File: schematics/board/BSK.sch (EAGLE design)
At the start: 56 parts

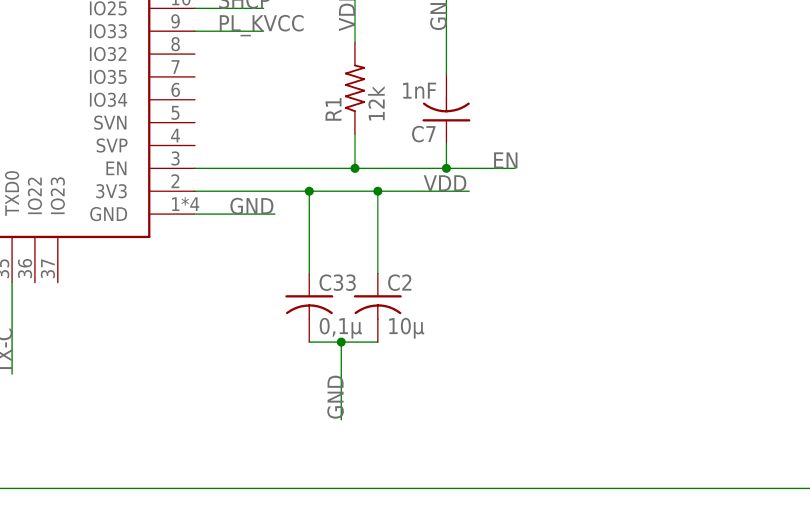
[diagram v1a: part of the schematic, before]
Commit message: Разведена плата БСК1
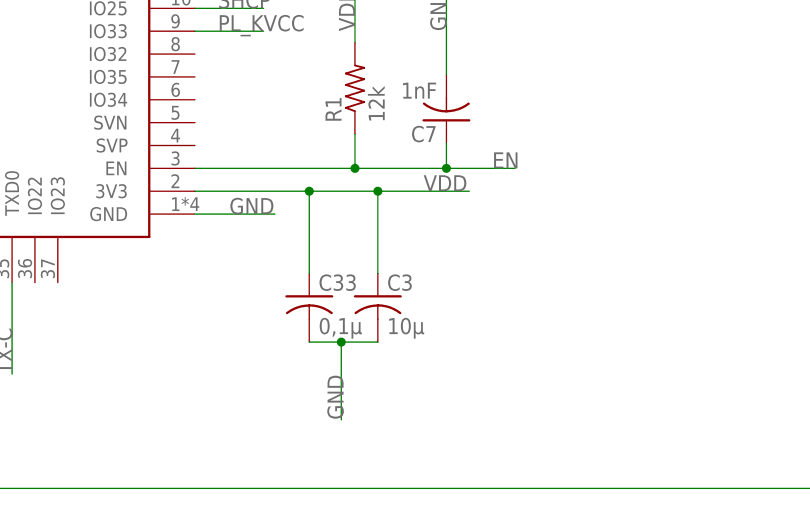
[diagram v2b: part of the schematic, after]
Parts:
- removed C2: 10µ, rcl:C-USC0603
- added C3: 10µ, rcl:C-USC1206
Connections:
- net GND: now also C3.2; no longer C2.2
- net VDD: now also C3.1; no longer C2.1
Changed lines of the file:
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@@
 </part>
 <part name="C33" library="rcl" library_urn="urn:adsk.eagle:library:334" deviceset="C-US" device="C0603" package3d_urn="urn:adsk.eagle:package:23616/2" value="0,1µ"/>
-<part name="C2" library="rcl" library_urn="urn:adsk.eagle:library:334" deviceset="C-US" device="C0603" package3d_urn="urn:adsk.eagle:package:23616/2" value="10µ"/>
 <part name="C7" library="rcl" library_urn="urn:adsk.eagle:library:334" deviceset="C-US" device="C0603" package3d_urn="urn:adsk.eagle:package:23616/2" value="1nF"/>
 <part name="R1" library="resistor" library_urn="urn:adsk.eagle:library:348" deviceset="R-US_" device="R0603" package3d_urn="urn:adsk.eagle:package:23555/3" value="12k"/>
@@
 <part name="LED-G#2" library="led" library_urn="urn:adsk.eagle:library:259" deviceset="LED" device="CHIPLED_0603" package3d_urn="urn:adsk.eagle:package:15822/2"/>
 <part name="R6" library="resistor" library_urn="urn:adsk.eagle:library:348" deviceset="R-US_" device="R0603" package3d_urn="urn:adsk.eagle:package:23555/3" value="2k"/>
+<part name="C3" library="rcl" library_urn="urn:adsk.eagle:library:334" deviceset="C-US" device="C1206" package3d_urn="urn:adsk.eagle:package:23618/2" value="10µ"/>
 </parts>
 <sheets>
@@
 <attribute name="VALUE" x="97.536" y="34.925" size="1.778" layer="96"/>
 </instance>
-<instance part="C2" gate="G$1" x="104.14" y="39.116" smashed="yes">
-<attribute name="NAME" x="105.156" y="39.751" size="1.778" layer="95"/>
-<attribute name="VALUE" x="105.156" y="34.925" size="1.778" layer="96"/>
-</instance>
 <instance part="C7" gate="G$1" x="111.76" y="58.674" smashed="yes" rot="R180">
 <attribute name="NAME" x="110.744" y="58.039" size="1.778" layer="95" rot="R180"/>
@@
 <attribute name="NAME" x="225.0186" y="105.41" size="1.778" layer="95" rot="R270"/>
 <attribute name="VALUE" x="220.218" y="105.41" size="1.778" layer="96" rot="R270"/>
+</instance>
+<instance part="C3" gate="G$1" x="104.14" y="39.116" smashed="yes">
+<attribute name="NAME" x="105.156" y="39.751" size="1.778" layer="95"/>
+<attribute name="VALUE" x="105.156" y="34.925" size="1.778" layer="96"/>
 </instance>
 </instances>
@@
 </segment>
 <segment>
-<pinref part="C2" gate="G$1" pin="2"/>
 <pinref part="C33" gate="G$1" pin="2"/>
 <wire x1="104.14" y1="34.036" x2="100.076" y2="34.036" width="0.1524" layer="91"/>
@@
 <junction x="100.076" y="34.036"/>
 <label x="100.33" y="25.4" size="1.778" layer="95" rot="R90"/>
+<pinref part="C3" gate="G$1" pin="2"/>
 </segment>
 <segment>
@@
 <junction x="104.14" y="50.8"/>
 <pinref part="C33" gate="G$1" pin="1"/>
-<pinref part="C2" gate="G$1" pin="1"/>
-</segment>
-<segment>
+<pinref part="C3" gate="G$1" pin="1"/>
+</segment>
+<segment>

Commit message: Исправлены компоненты
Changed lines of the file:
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@@
 <?xml version="1.0" encoding="utf-8"?>
 <!DOCTYPE eagle SYSTEM "eagle.dtd">
-<eagle version="9.5.1">
+<eagle version="9.6.0">
 <drawing>
 <settings>

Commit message: Исправлены АРК и БСК1
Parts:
- JTAG: device pinheadCS:PINHD-1X4 -> pinheadCS:PINHD-1X6
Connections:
- net GND: now also JTAG.1
- net MTCK: now also JTAG.5; no longer JTAG.3
- net MTDI: now also JTAG.6; no longer JTAG.4
- net MTDO: now also JTAG.3; no longer JTAG.1
- net MTMS: now also JTAG.4; no longer JTAG.2
- net VDD: now also JTAG.2
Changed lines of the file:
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@@
 <part name="R3" library="resistor" library_urn="urn:adsk.eagle:library:348" deviceset="R-US_" device="R0603" package3d_urn="urn:adsk.eagle:package:23555/3" value="2k"/>
 <part name="LED-B#3" library="led" library_urn="urn:adsk.eagle:library:259" deviceset="LED" device="CHIPLED_0603" package3d_urn="urn:adsk.eagle:package:15822/2"/>
-<part name="JTAG" library="pinheadCS" deviceset="PINHD-1X4" device=""/>
 <part name="LED-B#1" library="led" library_urn="urn:adsk.eagle:library:259" deviceset="LED" device="CHIPLED_0603" package3d_urn="urn:adsk.eagle:package:15822/2"/>
 <part name="R81" library="resistor" library_urn="urn:adsk.eagle:library:348" deviceset="R-US_" device="R0603" package3d_urn="urn:adsk.eagle:package:23555/3" value="2k"/>
@@
 <part name="R6" library="resistor" library_urn="urn:adsk.eagle:library:348" deviceset="R-US_" device="R0603" package3d_urn="urn:adsk.eagle:package:23555/3" value="2k"/>
 <part name="C3" library="rcl" library_urn="urn:adsk.eagle:library:334" deviceset="C-US" device="C1206" package3d_urn="urn:adsk.eagle:package:23618/2" value="10µ"/>
+<part name="JTAG" library="pinheadCS" deviceset="PINHD-1X6" device=""/>
 </parts>
 <sheets>
@@
 <attribute name="VALUE" x="19.685" y="35.052" size="1.778" layer="96" rot="R270"/>
 </instance>
-<instance part="JTAG" gate="A" x="55.88" y="129.54" smashed="yes" rot="R180">
-<attribute name="NAME" x="62.23" y="121.285" size="1.778" layer="95" rot="R180"/>
-<attribute name="VALUE" x="62.23" y="137.16" size="1.778" layer="96" rot="R180"/>
-</instance>
 <instance part="LED-B#1" gate="G$1" x="129.54" y="132.08" smashed="yes" rot="R180">
 <attribute name="NAME" x="125.222" y="139.7" size="1.778" layer="95" rot="R270"/>
@@
 <attribute name="NAME" x="105.156" y="39.751" size="1.778" layer="95"/>
 <attribute name="VALUE" x="105.156" y="34.925" size="1.778" layer="96"/>
+</instance>
+<instance part="JTAG" gate="A" x="55.88" y="127" smashed="yes" rot="R180">
+<attribute name="NAME" x="62.23" y="116.205" size="1.778" layer="95" rot="R180"/>
+<attribute name="VALUE" x="62.23" y="134.62" size="1.778" layer="96" rot="R180"/>
 </instance>
 </instances>
@@
 <junction x="198.12" y="78.74"/>
 </segment>
+<segment>
+<pinref part="JTAG" gate="A" pin="1"/>
+<wire x1="58.42" y1="119.38" x2="73.66" y2="119.38" width="0.1524" layer="91"/>
+<label x="66.04" y="119.38" size="1.778" layer="95"/>
+</segment>
 </net>
 <net name="5V" class="0">
@@
 <wire x1="25.4" y1="25.4" x2="25.4" y2="20.32" width="0.1524" layer="91"/>
 <wire x1="25.4" y1="26.67" x2="25.4" y2="27.94" width="0.1524" layer="91"/>
+</segment>
+<segment>
+<pinref part="JTAG" gate="A" pin="2"/>
+<wire x1="58.42" y1="121.92" x2="73.66" y2="121.92" width="0.1524" layer="91"/>
+<label x="66.04" y="121.92" size="1.778" layer="95"/>
 </segment>
 </net>
@@
 <net name="MTDI" class="0">
 <segment>
-<pinref part="JTAG" gate="A" pin="4"/>
 <wire x1="58.42" y1="132.08" x2="73.66" y2="132.08" width="0.1524" layer="91"/>
 <label x="66.04" y="132.08" size="1.778" layer="95"/>
+<pinref part="JTAG" gate="A" pin="6"/>
 </segment>
 <segment>
@@
 <net name="MTCK" class="0">
 <segment>
-<pinref part="JTAG" gate="A" pin="3"/>
 <wire x1="58.42" y1="129.54" x2="73.66" y2="129.54" width="0.1524" layer="91"/>
 <label x="66.04" y="129.54" size="1.778" layer="95"/>
+<pinref part="JTAG" gate="A" pin="5"/>
 </segment>
 <segment>
@@
 <net name="MTMS" class="0">
 <segment>
-<pinref part="JTAG" gate="A" pin="2"/>
 <wire x1="58.42" y1="127" x2="73.66" y2="127" width="0.1524" layer="91"/>
 <label x="66.04" y="127" size="1.778" layer="95"/>
+<pinref part="JTAG" gate="A" pin="4"/>
 </segment>
 <segment>
@@
 <net name="MTDO" class="0">
 <segment>
-<pinref part="JTAG" gate="A" pin="1"/>
 <wire x1="58.42" y1="124.46" x2="73.66" y2="124.46" width="0.1524" layer="91"/>
 <label x="66.04" y="124.46" size="1.778" layer="95"/>
-</segment>
-<segment>
+<pinref part="JTAG" gate="A" pin="3"/>
+</segment>
+<segment>

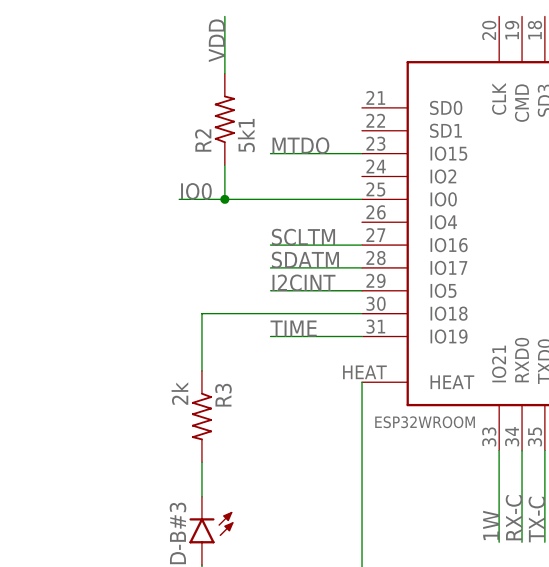
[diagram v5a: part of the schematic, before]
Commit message: Добавлены подтяжки i2c
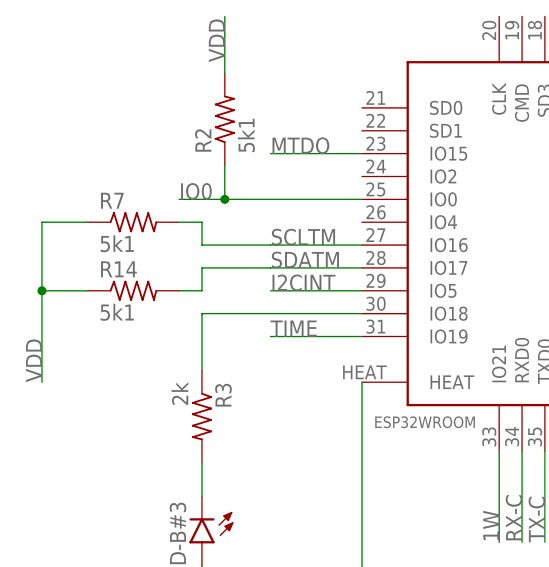
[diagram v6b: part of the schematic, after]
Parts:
- added R14, R7: 5k1, resistor:R-US_R0603
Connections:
- net SCLTM: now also R7.2
- net SDATM: now also R14.2
- net VDD: now also R14.1, R7.1

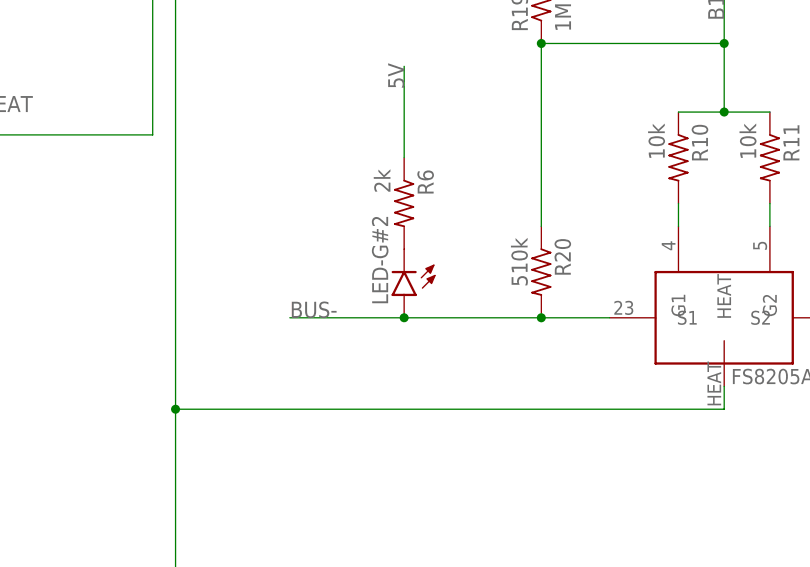
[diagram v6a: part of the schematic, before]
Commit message: Исправлены RADIO и диоды
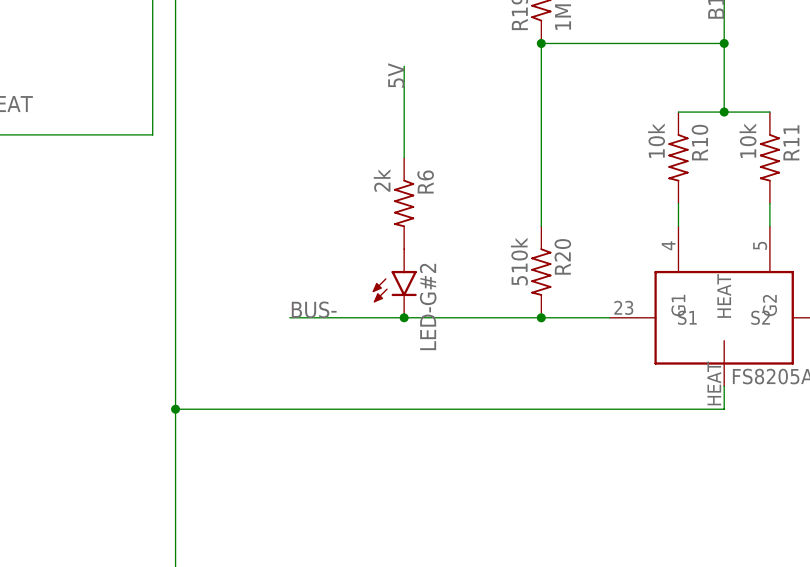
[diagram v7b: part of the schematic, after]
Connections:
- net BUS-: now also LED-G#2.C; no longer LED-G#2.A
- net N$38: now also LED-G#2.A; no longer LED-G#2.C
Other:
- moved on the sheet: LED-G#2
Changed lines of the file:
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@@
 <part name="R5" library="resistor" library_urn="urn:adsk.eagle:library:348" deviceset="R-US_" device="R0603" package3d_urn="urn:adsk.eagle:package:23555/3" value="2k"/>
 <part name="LED-B#2" library="led" library_urn="urn:adsk.eagle:library:259" deviceset="LED" device="CHIPLED_0603" package3d_urn="urn:adsk.eagle:package:15822/2"/>
-<part name="LED-G#2" library="led" library_urn="urn:adsk.eagle:library:259" deviceset="LED" device="CHIPLED_0603" package3d_urn="urn:adsk.eagle:package:15822/2"/>
 <part name="R6" library="resistor" library_urn="urn:adsk.eagle:library:348" deviceset="R-US_" device="R0603" package3d_urn="urn:adsk.eagle:package:23555/3" value="2k"/>
 <part name="C3" library="rcl" library_urn="urn:adsk.eagle:library:334" deviceset="C-US" device="C1206" package3d_urn="urn:adsk.eagle:package:23618/2" value="10µ"/>
@@
 <part name="R7" library="resistor" library_urn="urn:adsk.eagle:library:348" deviceset="R-US_" device="R0603" package3d_urn="urn:adsk.eagle:package:23555/3" value="5k1"/>
 <part name="R14" library="resistor" library_urn="urn:adsk.eagle:library:348" deviceset="R-US_" device="R0603" package3d_urn="urn:adsk.eagle:package:23555/3" value="5k1"/>
+<part name="LED-G#2" library="led" library_urn="urn:adsk.eagle:library:259" deviceset="LED" device="CHIPLED_0603" package3d_urn="urn:adsk.eagle:package:15822/2"/>
 </parts>
 <sheets>
@@
 <attribute name="VALUE" x="183.515" y="140.208" size="1.778" layer="96" rot="R90"/>
 </instance>
-<instance part="LED-G#2" gate="G$1" x="223.52" y="91.44" smashed="yes" rot="R180">
-<attribute name="NAME" x="219.964" y="100.33" size="1.778" layer="95" rot="R270"/>
-<attribute name="VALUE" x="217.805" y="96.012" size="1.778" layer="96" rot="R270"/>
-</instance>
 <instance part="R6" gate="G$1" x="223.52" y="101.6" smashed="yes" rot="R270">
 <attribute name="NAME" x="225.0186" y="105.41" size="1.778" layer="95" rot="R270"/>
@@
 <attribute name="NAME" x="13.97" y="59.9186" size="1.778" layer="95"/>
 <attribute name="VALUE" x="13.97" y="55.118" size="1.778" layer="96"/>
+</instance>
+<instance part="LED-G#2" gate="G$1" x="223.52" y="93.98" smashed="yes">
+<attribute name="NAME" x="227.076" y="85.09" size="1.778" layer="95" rot="R90"/>
+<attribute name="VALUE" x="229.235" y="89.408" size="1.778" layer="96" rot="R90"/>
 </instance>
 </instances>
@@
 <label x="210.82" y="88.9" size="1.778" layer="95"/>
 <pinref part="FS8205A" gate="G$1" pin="S1"/>
-<pinref part="LED-G#2" gate="G$1" pin="A"/>
+<pinref part="LED-G#2" gate="G$1" pin="C"/>
 <wire x1="223.52" y1="88.9" x2="210.82" y2="88.9" width="0.1524" layer="91"/>
 <junction x="223.52" y="88.9"/>
@@
 <net name="N$38" class="0">
 <segment>
+<pinref part="LED-G#2" gate="G$1" pin="A"/>
 <pinref part="R6" gate="G$1" pin="2"/>
-<pinref part="LED-G#2" gate="G$1" pin="C"/>
-</segment>
-</net>
+</segment>
+</net>

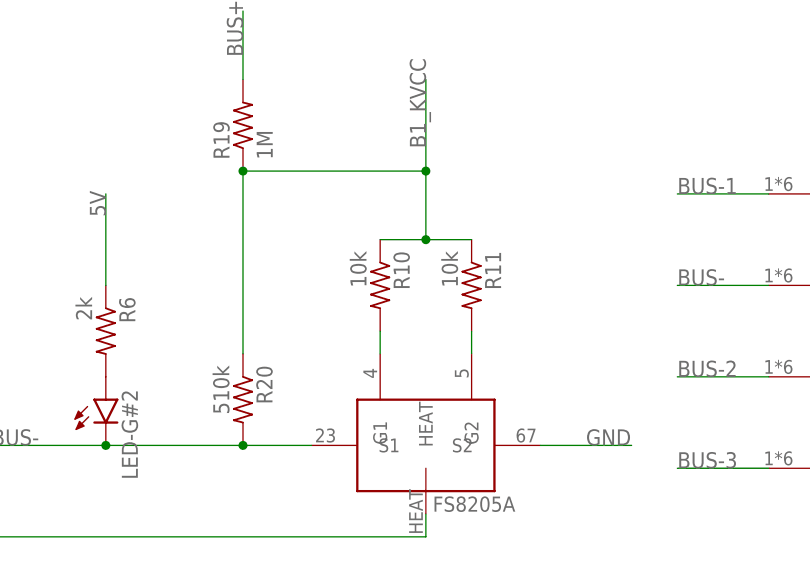
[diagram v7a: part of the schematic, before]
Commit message: Резисторы у FS8205A 100Ом
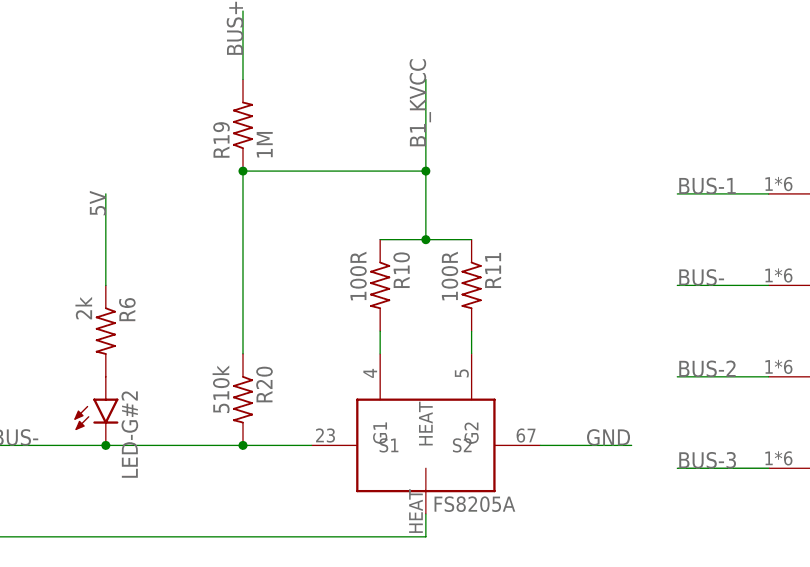
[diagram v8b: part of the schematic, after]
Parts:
- R10, R11: value 10k -> 100R
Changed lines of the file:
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@@
 <part name="U$13" library="CanCubeSat" deviceset="ESP32WROOM" device=""/>
 <part name="74HC595#1" library="CanCubeSat" deviceset="74HC595" device=""/>
-<part name="R10" library="resistor" library_urn="urn:adsk.eagle:library:348" deviceset="R-US_" device="R0603" package3d_urn="urn:adsk.eagle:package:23555/3" value="10k"/>
-<part name="R11" library="resistor" library_urn="urn:adsk.eagle:library:348" deviceset="R-US_" device="R0603" package3d_urn="urn:adsk.eagle:package:23555/3" value="10k"/>
+<part name="R10" library="resistor" library_urn="urn:adsk.eagle:library:348" deviceset="R-US_" device="R0603" package3d_urn="urn:adsk.eagle:package:23555/3" value="100R"/>
+<part name="R11" library="resistor" library_urn="urn:adsk.eagle:library:348" deviceset="R-US_" device="R0603" package3d_urn="urn:adsk.eagle:package:23555/3" value="100R"/>
 <part name="R19" library="resistor" library_urn="urn:adsk.eagle:library:348" deviceset="R-US_" device="R0603" package3d_urn="urn:adsk.eagle:package:23555/3" value="1M"/>
 <part name="R20" library="resistor" library_urn="urn:adsk.eagle:library:348" deviceset="R-US_" device="R0603" package3d_urn="urn:adsk.eagle:package:23555/3" value="510k"/>
